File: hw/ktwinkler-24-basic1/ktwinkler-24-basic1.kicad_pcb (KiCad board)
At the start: 4 copper layers, 64 x 58 mm, 97 parts, among them J1 USB_C_Receptacle_USB2.0_16P, J10 Conn_01x06, J11 Conn_01x02, J12 Connector_HAN_P1, J13 Conn_01x02, J14 Conn_01x02, J15 Conn_01x02, J16 Conn_01x02, J17 Conn_01x02, J18 Conn_01x02, J19 Conn_01x06, J2 Conn_01x02, J3 Conn_01x04, J4 Conn_01x02, J5 Conn_01x03, J6 Conn_01x02, J7 Conn_01x02, J8 Conn_01x02, J9 BWU.FL-IPEX1, Q1 HL3400A, Q3 HL2301A, Q4 HL3400A, SW1 RESET, SW2 BOOT, SW5 MODE, U1 TPS631000DRLR, U2 FM116C, U3 ESP32-C3FH4, U4 T1016H, U5 AD116, U6 Protection_H5VU25UC, U8 CH584F, U9 GM8023B, Y1 40M, Y2 32k, Y4 32k, Y5 32M

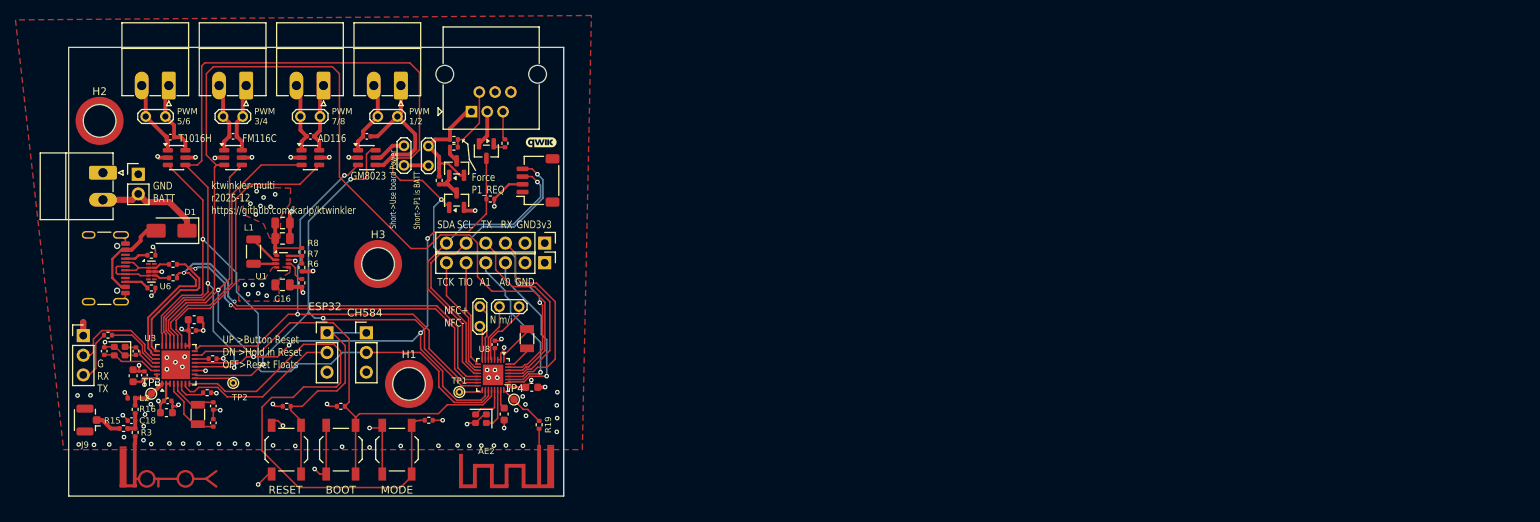
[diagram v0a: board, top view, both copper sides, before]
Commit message: k24: rough blocked, fixed old values for bucks
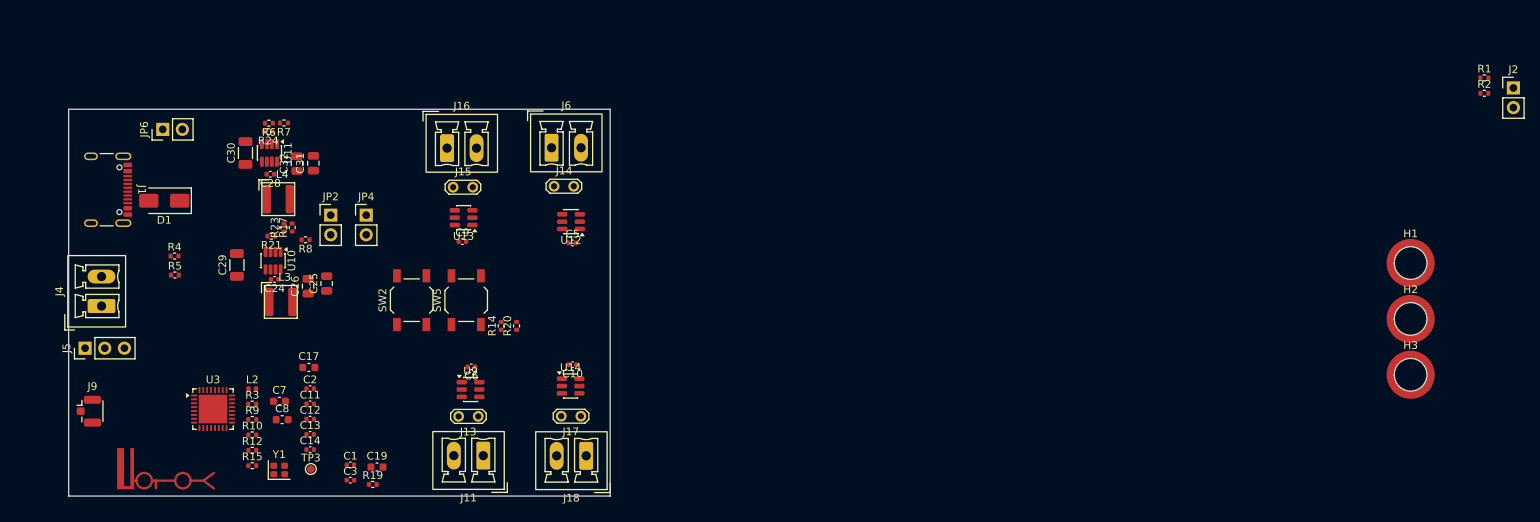
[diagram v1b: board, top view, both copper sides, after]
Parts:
- removed AE2: Antenna_Loop, wch-antenna:ANT-F-1-2.4G-1.6MM-FR4-WCH-FLIP
- removed C15, C16: 22uF, Capacitor_SMD:C_0805_2012Metric
- removed C18: 2.2pF, Capacitor_SMD:C_0402_1005Metric
- removed C20, C4: 100nF, Capacitor_SMD:C_0402_1005Metric
- removed C22: 1uF, Capacitor_SMD:C_0603_1608Metric
- removed G1: qwiic_Logo, SparkFun-Qwiic:qwiic_4mm
- removed J10, J19: Conn_01x06, Connector_PinHeader_2.54mm:PinHeader_1x06_P2.54mm_Vertical
- removed J12: Connector_HAN_P1, Connector_RJ:RJ25_Wayconn_MJEA-660X1_Horizontal
- removed J3: Conn_01x04, Connector_JST:JST_SH_SM04B-SRSS-TB_1x04-1MP_P1.00mm_Horizontal
- removed J7, J8: Conn_01x02, Connector_Phoenix_MC:PhoenixContact_MC_1,5_2-G-3.5_1x02_P3.50mm_Horizontal
- removed JP1: KJumper_3, Connector_PinHeader_2.54mm:PinHeader_1x03_P2.54mm_Vertical
- removed JP3: LocalPower, TestPoint:TestPoint_2Pads_Pitch2.54mm_Drill0.8mm
- removed L1: 1uH, Inductor_SMD:L_1206_3216Metric
- removed Q1, Q4: HL3400A, Package_TO_SOT_SMD:SOT-23
- removed Q3: HL2301A, Package_TO_SOT_SMD:SOT-23
- removed R11, R18, R22: 10k, Resistor_SMD:R_0402_1005Metric
- removed R13, R16: 0R, Resistor_SMD:R_0402_1005Metric
- removed SW1: RESET, Button_Switch_SMD:SW_SPST_TL3342
- removed TP1, TP2: TestPoint, TestPoint:TestPoint_THTPad_D1.0mm_Drill0.5mm
- removed TP4: TestPoint, TestPoint:TestPoint_Pad_D1.0mm
- removed U1: TPS631000DRLR, Package_TO_SOT_SMD:SOT-583-8
- removed U2: FM116C, Package_TO_SOT_SMD:SOT-23-6
- removed U4: T1016H, Package_TO_SOT_SMD:SOT-23-6
- removed U5: AD116, Package_TO_SOT_SMD:SOT-23-6
- removed U6: Protection_H5VU25UC, Package_DFN_QFN:Diodes_UDFN-10_1.0x2.5mm_P0.5mm
- removed U8: CH584F, Package_DFN_QFN:QFN-32-1EP_4x4mm_P0.4mm_EP2.65x2.65mm
- removed Y2, Y4: 32k, Crystal:Crystal_SMD_3215-2Pin_3.2x1.5mm
- removed Y5: 32M, Crystal:Crystal_SMD_2016-4Pin_2.0x1.6mm
- added C24: 10nF, Capacitor_SMD:C_0402_1005Metric, F.Cu at (126.6, 122.0)
- added C25: 22uF, Capacitor_SMD:C_0805_2012Metric, F.Cu at (133.3, 122.5)
- added C26: 22uF, Capacitor_SMD:C_0805_2012Metric, F.Cu at (130.9, 122.9)
- added C28: 10nF, Capacitor_SMD:C_0402_1005Metric, F.Cu at (126.1, 108.4)
- added C29: 10uF, Capacitor_SMD:C_1206_3216Metric, F.Cu at (121.8, 120.1)
- added C30: 10uF, Capacitor_SMD:C_1206_3216Metric, F.Cu at (122.9, 105.7)
- added C31: 22uF, Capacitor_SMD:C_0805_2012Metric, F.Cu at (131.6, 107.0)
- added C32: 22uF, Capacitor_SMD:C_0805_2012Metric, F.Cu at (129.5, 107.0)
- added JP6: KJumper_2, Connector_PinHeader_2.54mm:PinHeader_1x02_P2.54mm_Vertical, F.Cu at (112.2, 102.6)
- added L3: 2u2, et-parts:L_Changjiang_FNR4030S, F.Cu at (127.4, 124.9)
- added L4: 2u2, et-parts:L_Changjiang_FNR4030S, F.Cu at (127.1, 111.6)
- added R23: 20k, Resistor_SMD:R_0402_1005Metric, F.Cu at (127.8, 115.3)
- added R24: 470R, Resistor_SMD:R_0402_1005Metric, F.Cu at (125.8, 102.9)
- added U10: SY8303, Package_TO_SOT_SMD:TSOT-23-8, F.Cu at (126.4, 119.6)
- added U11: SY8303, Package_TO_SOT_SMD:TSOT-23-8, F.Cu at (126.0, 105.6)
- added U12: GM8023B, Package_TO_SOT_SMD:SOT-23-6, F.Cu at (164.9, 114.5)
- added U13: GM8023B, Package_TO_SOT_SMD:SOT-23-6, F.Cu at (151.1, 114.0)
- added U14: GM8023B, Package_TO_SOT_SMD:SOT-23-6, F.Cu at (164.9, 135.8)
- C1: value 22uF -> 1.5pf; footprint Capacitor_SMD:C_0805_2012Metric -> Capacitor_SMD:C_0402_1005Metric
- C10, C9: value 22pF -> 100nF
- C3: value 100nF -> 1.5pf
- J11, J4, J6: footprint Connector_Phoenix_MC:PhoenixContact_MC_1,5_2-G-3.5_1x02_P3.50mm_Horizontal -> Connector_Phoenix_MC:PhoenixContact_MCV_1,5_2-G-3.81_1x02_P3.81mm_Vertical
- J16, J18: footprint TestPoint:TestPoint_2Pads_Pitch2.54mm_Drill0.8mm -> Connector_Phoenix_MC:PhoenixContact_MCV_1,5_2-G-3.81_1x02_P3.81mm_Vertical
- JP2: value KJumper_3 -> KJumper_2; footprint Connector_PinHeader_2.54mm:PinHeader_1x03_P2.54mm_Vertical -> Connector_PinHeader_2.54mm:PinHeader_1x02_P2.54mm_Vertical
- JP4: footprint TestPoint:TestPoint_2Pads_Pitch2.54mm_Drill0.8mm -> Connector_PinHeader_2.54mm:PinHeader_1x02_P2.54mm_Vertical
- L2: value 1nH -> 2.2nH
- R17: value 0R -> 7k5
- R19: value 0R -> 10k
- R21: value 0R -> 470R
- R6: value 10k -> 33k
- R7: value 39k -> 150k
- R8: value 220k -> 150k
- moved J2 178.1 mm to (286.8, 97.2)
- moved R2 174.1 mm to (283.0, 97.9)
- moved R1 173.8 mm to (283.0, 95.9)
- moved H2 171.4 mm to (273.5, 127.1)
- moved H3 134.2 mm to (273.5, 134.3)
- moved H1 130.4 mm to (273.5, 119.9)
- moved J11 49.0 mm to (153.6, 144.8)
- moved C10 46.7 mm to (165.1, 133.0), turned to 180 degrees
- moved C5 46.0 mm to (165.1, 117.3), turned to 0 degrees
- moved C3 44.7 mm to (136.4, 147.9), turned to 0 degrees
- moved J14 41.2 mm to (162.8, 110.0), turned to 0 degrees
- moved J6 40.3 mm to (162.4, 105.0), turned to 0 degrees
- moved J13 40.2 mm to (152.9, 139.7)
- moved C9 39.8 mm to (150.9, 117.1), turned to 0 degrees
- moved J15 38.3 mm to (149.7, 110.1), turned to 0 degrees
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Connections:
- net /ch584/PWM2 renamed /esp32/PWM2
- net Net-(U3-GPIO2) renamed /esp32/PWM6
- net Net-(U3-GPIO8) renamed /esp32/PWM5
- C1 pad 1: +3V3 -> Net-(C1-Pad1)
- C10 pad 1: GND -> Net-(J17-Pin_1)
- C10 pad 2: Net-(U3-XTAL_32K_N) -> Net-(J17-Pin_2)
- C19 pad 1: Net-(U8B-VDCIA) -> Net-(U3-CHIP_EN)
- C3 pad 1: Net-(J16-Pin_1) -> Net-(U3-LNA_IN)
- C3 pad 2: Net-(J16-Pin_2) -> GND
- C9 pad 1: GND -> Net-(J15-Pin_1)
- C9 pad 2: Net-(U3-XTAL_32K_P) -> Net-(J15-Pin_2)
- D1 pad 1: +BATT -> +VDC
- D1 pad 2: /power/VBUS -> VBUS
- J1 pad A4: /power/VBUS -> VBUS
- J1 pad A9: /power/VBUS -> VBUS
- J1 pad B4: /power/VBUS -> VBUS
- J1 pad B9: /power/VBUS -> VBUS
- J16 pad 1: Net-(J16-Pin_1) -> Net-(J15-Pin_1)
- J16 pad 2: Net-(J16-Pin_2) -> Net-(J15-Pin_2)
- J17 pad 1: /ch584/nfc_i -> Net-(J17-Pin_1)
- J17 pad 2: /ch584/nfc_m -> Net-(J17-Pin_2)
- J18 pad 1: /ch584/nfc- -> Net-(J17-Pin_1)
- J18 pad 2: /ch584/nfc+ -> Net-(J17-Pin_2)
- J2 pad 2: +BATT -> +VDC
- J4 pad 2: +BATT -> +VDC
- JP2 pad 1: /RESET_GLOBAL -> Net-(JP2-A)
- JP2 pad 2: RESET_CH5x -> Net-(JP2-B)
- JP4 pad 1: +5V -> Net-(JP4-A)
- JP4 pad 2: +BATT -> Net-(JP2-B)
- L2 pad 1: GND -> Net-(U3-LNA_IN)
- L2 pad 2: Net-(U3-LNA_IN) -> Net-(C1-Pad1)
- R15 pad 2: Net-(C18-Pad1) -> Net-(C1-Pad1)
- R17 pad 1: /ScopeCreep/P1_OUT_RAW -> Net-(JP4-A)
- R17 pad 2: Net-(Q4-G) -> GND
- R19 pad 1: Net-(U8B-ANT) -> Net-(U3-CHIP_EN)
- R19 pad 2: Net-(AE2-Pad1) -> +3V3
- R21 pad 1: /ScopeCreep/P1_REQ -> Net-(U10-FS)
- R21 pad 2: Net-(Q3-D) -> GND
- R3 pad 1: Net-(C18-Pad1) -> Net-(C1-Pad1)
- R6 pad 1: GND -> Net-(U11-FB)
- R6 pad 2: Net-(U1-MODE) -> GND
- R7 pad 1: Net-(U1-FB) -> +3.3V
- R7 pad 2: GND -> Net-(U11-FB)
- R8 pad 1: +3V3 -> VBUS
- R8 pad 2: Net-(U1-FB) -> Net-(JP2-B)
- U3 pad 12: /ch584/PWM5 -> /esp32/PWM7
- U3 pad 13: /ch584/PWM3 -> /esp32/PWM8
- U3 pad 16: /ch584/PWM1 -> unconnected-(U3-GPIO10-Pad16)
- U3 pad 19: /esp32/PWM7 -> unconnected-(U3-SPIHD-Pad19)
- U3 pad 20: /esp32/PWM8 -> unconnected-(U3-SPIWP-Pad20)
- U3 pad 21: /ch584/PWM3 -> unconnected-(U3-SPICS0-Pad21)
- U3 pad 22: /ch584/PWM4 -> unconnected-(U3-SPICLK-Pad22)
- U3 pad 23: /ch584/PWM5 -> unconnected-(U3-SPID-Pad23)
- U3 pad 24: RESET_CH5x -> unconnected-(U3-SPIQ-Pad24)
- U3 pad 4: Net-(U3-XTAL_32K_P) -> /esp32/PWM3
- U3 pad 5: Net-(U3-XTAL_32K_N) -> /esp32/PWM4
- U3 pad 7: RESET_ESP -> Net-(U3-CHIP_EN)
- U3 pad 9: Net-(U3-MTMS) -> /esp32/PWM1
- U9 pad 3: /ch584/PWM1 -> /esp32/PWM1
- U9 pad 5: Net-(JP3-B) -> VBUS
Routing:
- net /ch584/PWM5: track 151.1 -> 0.00 mm, vias 4 -> 0
- net /ch584/PWM4: track 122.7 -> 0.00 mm
- net /ch584/PWM3: track 114.6 -> 0.00 mm, vias 5 -> 0
- net RESET_CH5x: track 84.6 -> 0.00 mm, vias 1 -> 0
- net /MODE: track 74.5 -> 0.00 mm
- net /esp32/PWM2: track 72.0 -> 0.00 mm, vias 3 -> 0
- net GND: track 71.3 -> 0.00 mm, vias 73 -> 0
- net /ch584/PWM1: track 66.4 -> 0.00 mm, vias 2 -> 0
- net USBDP: track 66.4 -> 0.00 mm, vias 2 -> 0
- net USBDN: track 65.0 -> 0.00 mm, vias 2 -> 0
- net GBOOT: track 61.3 -> 0.00 mm
- net /ch584/TWI_SCL: track 40.2 -> 0.00 mm, vias 1 -> 0
- net /ch584/TWI_SDA: track 39.8 -> 0.00 mm, vias 1 -> 0
- net /esp32/PWM7: track 36.7 -> 0.00 mm
- net /esp32/PWM8: track 35.5 -> 0.00 mm
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- removed copper zone on F.Cu, net +3V3
- removed copper zone on In2.Cu, net +3V3
- removed copper zone on F.Cu, net +BATT
- removed copper zone on In2.Cu, net +BATT
- removed copper zone on F.Cu, net GND
- removed copper zone on In1.Cu, net GND
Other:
- board size 64 x 58 mm -> 70 x 50 mm
- board text removed: "3v3"
- board text removed: "A0"
- board text removed: "A1"
- board text removed: "AD116"
- board text removed: "BOOT"
- board text removed: "CH584"
- board text removed: "ESP32"
- board text removed: "FM116C"
- board text removed: "Force P1_REQ"
- board text removed: "G RX TX"
- board text removed: "GM8023"
- board text removed: "GND"
- board text removed: "GND BATT"
- board text removed: "MODE"
- board text removed: "N m/i"
- board text removed: "NFC+ NFC-"
- board text removed: "PWM 1/2"
- board text removed: "PWM 3/4"
- board text removed: "PWM 5/6"
- board text removed: "PWM 7/8"
- board text removed: "RESET"
- board text removed: "RX"
- board text removed: "SCL"
- board text removed: "SDA"
- board text removed: "Short->P1 is BATT"
- board text removed: "Short->Use board Power"
- board text removed: "T1016H"
- board text removed: "TCK"
- board text removed: "TIO"
- board text removed: "TX"
- board text removed: "UP >Button Reset DN >Hold in Reset OFF>Reset Floats"
- board text removed: "ktwinkler-multi r2025-12 https://github.com/karlp/ktwinkler"

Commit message: k24-basic1: first cut layout complete
re(un)twisted all the outputs to be straight.
seems like this is all it needs... yolo?
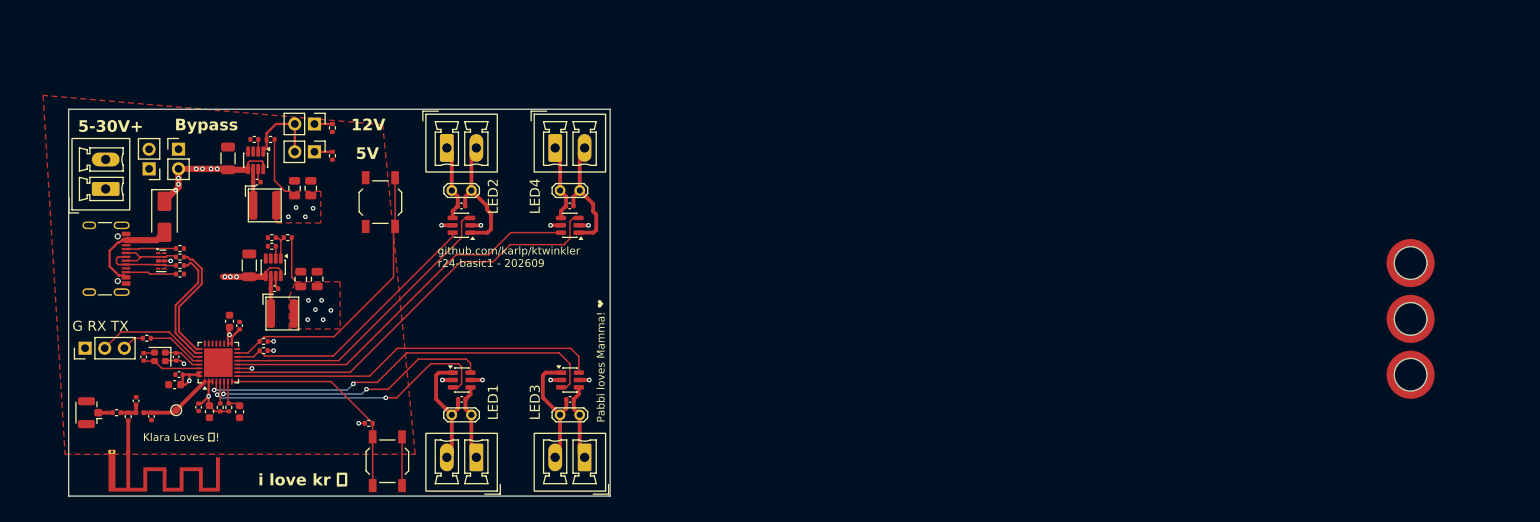
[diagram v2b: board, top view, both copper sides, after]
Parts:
- added U6: Protection_H5VU25UC, Package_DFN_QFN:Diodes_UDFN-10_1x2.5mm_P0.5mm, F.Cu at (112.0, 119.6)
- AE1: footprint RF_Experiments:ANT-YOLOPOLE -> RF_Antenna:Texas_SWRA117D_2.4GHz_Left
- moved J2 176.7 mm to (110.4, 107.7), turned to 180 degrees
- moved R2 170.2 mm to (114.4, 121.3)
- moved R1 170.1 mm to (114.4, 118.0)
- moved R20 32.8 mm to (125.2, 130.0), turned to 180 degrees
- moved C1 28.9 mm to (108.7, 137.7), turned to 90 degrees
- moved C3 27.0 mm to (110.7, 139.7), turned to -90 degrees
- moved SW5 23.2 mm to (141.2, 145.5), turned to -90 degrees
- moved C11 22.4 mm to (109.7, 132.0), turned to 90 degrees
- moved Y1 21.3 mm to (111.8, 132.0), turned to 180 degrees
- moved R14 21.2 mm to (138.8, 140.6), turned to 0 degrees
- moved R19 21.1 mm to (120.7, 138.5), turned to -90 degrees
- moved C14 19.5 mm to (114.3, 134.3), turned to 180 degrees
- moved C19 19.1 mm to (122.1, 139.1), turned to -90 degrees
- moved C12 19.1 mm to (113.9, 132.0), turned to -90 degrees
- moved TP3 19.0 mm to (113.9, 138.9)
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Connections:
- net Net-(J11-Pin_1) renamed /leds/out1a
- net Net-(J11-Pin_2) renamed /leds/out1b
- net Net-(J14-Pin_1) renamed /leds/out4a
- net Net-(J14-Pin_2) renamed /leds/out4b
- net Net-(J15-Pin_1) renamed /leds/out2a
- net Net-(J15-Pin_2) renamed /leds/out2b
- net Net-(J17-Pin_1) renamed /leds/out3a
- net Net-(J17-Pin_2) renamed /leds/out3b
- net Net-(J5-Pin_2) renamed /esp32/U0RXD
- net Net-(J5-Pin_3) renamed /esp32/U0TXD
- net Net-(U3-U0TXD) renamed /esp32/U0TXDb
- C31 pad 1: +3.3V -> +3V3
- C32 pad 1: +3.3V -> +3V3
- D1 pad 2: VBUS -> /power/VUBus
- J1 pad A4: VBUS -> /power/VUBus
- J1 pad A9: VBUS -> /power/VUBus
- J1 pad B4: VBUS -> /power/VUBus
- J1 pad B9: VBUS -> /power/VUBus
- L4 pad 2: +3.3V -> +3V3
- R10 pad 2: /esp32/PWM6 -> /esp32/PWM2
- R12 pad 2: /esp32/PWM5 -> /esp32/PWM4
- R7 pad 1: +3.3V -> +3V3
- U12 pad 3: /esp32/PWM3 -> /esp32/PWM7
- U12 pad 6: /esp32/PWM4 -> /esp32/PWM8
- U13 pad 3: /esp32/PWM5 -> /esp32/PWM3
- U13 pad 6: /esp32/PWM6 -> /esp32/PWM4
- U14 pad 3: /esp32/PWM7 -> /esp32/PWM5
- U14 pad 6: /esp32/PWM8 -> /esp32/PWM6
- U3 pad 10: /esp32/PWM2 -> /esp32/PWM7
- U3 pad 12: /esp32/PWM7 -> /esp32/PWM8
- U3 pad 13: /esp32/PWM8 -> /esp32/PWM3
- U3 pad 14: /esp32/PWM5 -> /esp32/PWM4
- U3 pad 4: /esp32/PWM3 -> /esp32/PWM5
- U3 pad 5: /esp32/PWM4 -> /esp32/PWM1
- U3 pad 6: /esp32/PWM6 -> /esp32/PWM2
- U3 pad 9: /esp32/PWM1 -> /esp32/PWM6
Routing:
- net /esp32/PWM7: track 0.00 -> 53.7 mm
- net /esp32/PWM5: track 0.00 -> 53.7 mm, vias 0 -> 2
- net /esp32/PWM8: track 0.00 -> 48.9 mm
- net /esp32/PWM6: track 0.00 -> 48.2 mm
- net /esp32/PWM1: track 0.00 -> 39.1 mm, vias 0 -> 2
- net /esp32/PWM3: track 0.00 -> 39.0 mm
- net /esp32/PWM2: track 0.00 -> 38.3 mm, vias 0 -> 2
- net GBOOT: track 0.00 -> 37.2 mm
- net /esp32/PWM4: track 0.00 -> 35.4 mm
- net +3V3: track 0.00 -> 32.2 mm, vias 0 -> 13
- net /MODE: track 0.00 -> 28.5 mm
- net +VDC: track 0.00 -> 26.8 mm, vias 0 -> 10
- net GND: track 0.00 -> 17.3 mm, vias 0 -> 6
- net /leds/out2b: track 0.00 -> 17.0 mm
- net /leds/out3b: track 0.00 -> 16.6 mm
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- added copper zone on F.Cu, net +3V3
- added copper zone on In2.Cu, net +3V3
- added copper zone on In2.Cu, net +VDC
- added copper zone on F.Cu, net GND
- added copper zone on In1.Cu, net GND
- added copper zone on F.Cu, net VBUS
- added copper zone on In2.Cu, net VBUS
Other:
- board text added: "12V"
- board text added: "5-30V+"
- board text added: "5V"
- board text added: "Bypass"
- board text added: "G RX TX"
- board text added: "Klara Loves 🍨!"
- board text added: "LED1"
- board text added: "LED2"
- board text added: "LED3"
- board text added: "LED4"
- board text added: "Pabbi loves Mamma! ❤️"
- board text added: "github.com/karlp/ktwinkler r24-basic1 - 202609"
- board text added: "i love kr ⚽"

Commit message: 24-1: connect some planes that were independent
other little tidy ups
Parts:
- removed H1, H2, H3: Mounting_SMTSO3015CTJ, jlc-extras:Mounting_SMTSO_M3_ALT2
- moved C30 0.35 mm to (123.0, 120.2)
- moved R21 0.30 mm to (124.0, 103.6)
- moved R8 0.30 mm to (126.1, 103.6)
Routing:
- net GND: track 17.3 -> 18.6 mm, vias 6 -> 40

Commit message: k24-1: mounting, rounding labels
save point before retrying thigns
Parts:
- added H1: MountingHole, MountingHole:MountingHole_3.2mm_M3, F.Cu at (141.6, 145.9)
- added H2: MountingHole, MountingHole:MountingHole_3.2mm_M3, F.Cu at (163.6, 123.0)
- added H3: MountingHole, MountingHole:MountingHole_3.2mm_M3, F.Cu at (118.7, 114.2)
- added TP4: TestPoint, TestPoint:TestPoint_Pad_D1.0mm, F.Cu at (122.4, 124.8)
- added X1: ~, jlc-extras:JLC_2D_BARCODE_8x8mm, F.Cu at (149.2, 127.7)
- moved SW5 7.26 mm to (140.3, 138.3), turned to 180 degrees
- moved R14 5.10 mm to (135.3, 136.9), turned to 90 degrees
- moved C10 2.40 mm to (162.4, 137.5)
- moved C5 2.40 mm to (162.4, 112.5)
- moved J14 2.40 mm to (161.1, 110.5)
- moved J17 2.40 mm to (163.7, 139.5)
- moved U12 2.40 mm to (162.4, 115.0)
- moved U14 2.40 mm to (162.4, 135.0)
- moved J18 2.40 mm to (164.3, 145.0)
- moved J6 2.40 mm to (160.5, 105.0)
- moved SW2 1.10 mm to (140.3, 110.9), turned to 180 degrees
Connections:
- J1 pad SH: (no net) -> GND
- U3 pad 16: unconnected-(U3-GPIO10-Pad16) -> Net-(U3-GPIO10)
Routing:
- net Net-(U3-GPIO10): track 0.00 -> 7.84 mm
- net GND: track 18.6 -> 12.3 mm, vias 40 -> 37
- net /MODE: track 28.5 -> 22.8 mm
- net GBOOT: track 37.2 -> 41.5 mm
- net /esp32/PWM7: track 53.7 -> 51.3 mm
- net /esp32/PWM5: track 53.7 -> 51.3 mm
- net /esp32/PWM6: track 48.2 -> 45.8 mm
- net /esp32/PWM8: track 48.9 -> 46.5 mm
- net /esp32/PWM3: track 39.0 -> 37.9 mm

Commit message: 24-basic1: ordered and sent off
sw time!
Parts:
- moved H1 19.8 mm to (161.4, 146.4)
- moved H2 19.5 mm to (161.4, 103.6)
- moved J18 16.8 mm to (160.3, 128.7), turned to -90 degrees
- moved SW5 14.7 mm to (153.1, 145.5), turned to 90 degrees
- moved SW2 14.3 mm to (153.1, 104.4), turned to 90 degrees
- moved J17 13.5 mm to (154.8, 129.3), turned to -90 degrees
- moved U12 13.0 mm to (150.2, 119.5), turned to 90 degrees
- moved U14 12.9 mm to (150.3, 130.6), turned to 90 degrees
- moved J6 12.6 mm to (160.2, 117.6), turned to -90 degrees
- moved C5 11.9 mm to (152.7, 119.5), turned to -90 degrees
- moved C10 11.9 mm to (152.8, 130.6), turned to -90 degrees
- moved J14 10.0 mm to (154.7, 118.2), turned to -90 degrees
- moved X1 9.14 mm to (141.3, 123.1)
- moved C6 6.22 mm to (144.6, 137.5)
- moved J11 6.22 mm to (146.5, 145.0)
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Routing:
- net /MODE: track 22.8 -> 47.6 mm
- net GBOOT: track 41.5 -> 65.9 mm
- net /esp32/PWM6: track 45.8 -> 29.6 mm
- net /esp32/PWM7: track 51.3 -> 36.2 mm
- net /esp32/PWM5: track 51.3 -> 36.9 mm
- net /esp32/PWM8: track 46.5 -> 33.5 mm
- net /esp32/PWM2: track 38.3 -> 31.1 mm
- net GND: track 12.3 -> 19.1 mm, vias 37 -> 41
- net /esp32/PWM1: track 39.1 -> 32.8 mm
- net +3V3: track 32.6 -> 36.2 mm, vias 13 -> 17
- net /esp32/PWM4: track 35.1 -> 32.0 mm
- net /esp32/PWM3: track 37.9 -> 35.3 mm
- net /leds/out2b: track 17.0 -> 15.2 mm
- net /leds/out1b: track 16.4 -> 17.1 mm
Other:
- board size 70 x 50 mm -> 65 x 50 mm
- board text added: "3v3"
- board text added: "BT"
- board text added: "SW"
- board text added: "Vbus"
